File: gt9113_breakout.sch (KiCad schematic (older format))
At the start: 8 parts, among them J1 Conn_01x04_Male, J2 10118194-0001LF, J7 504740-5100, J8 504740-5100, U2 HT7533-1-SOT89

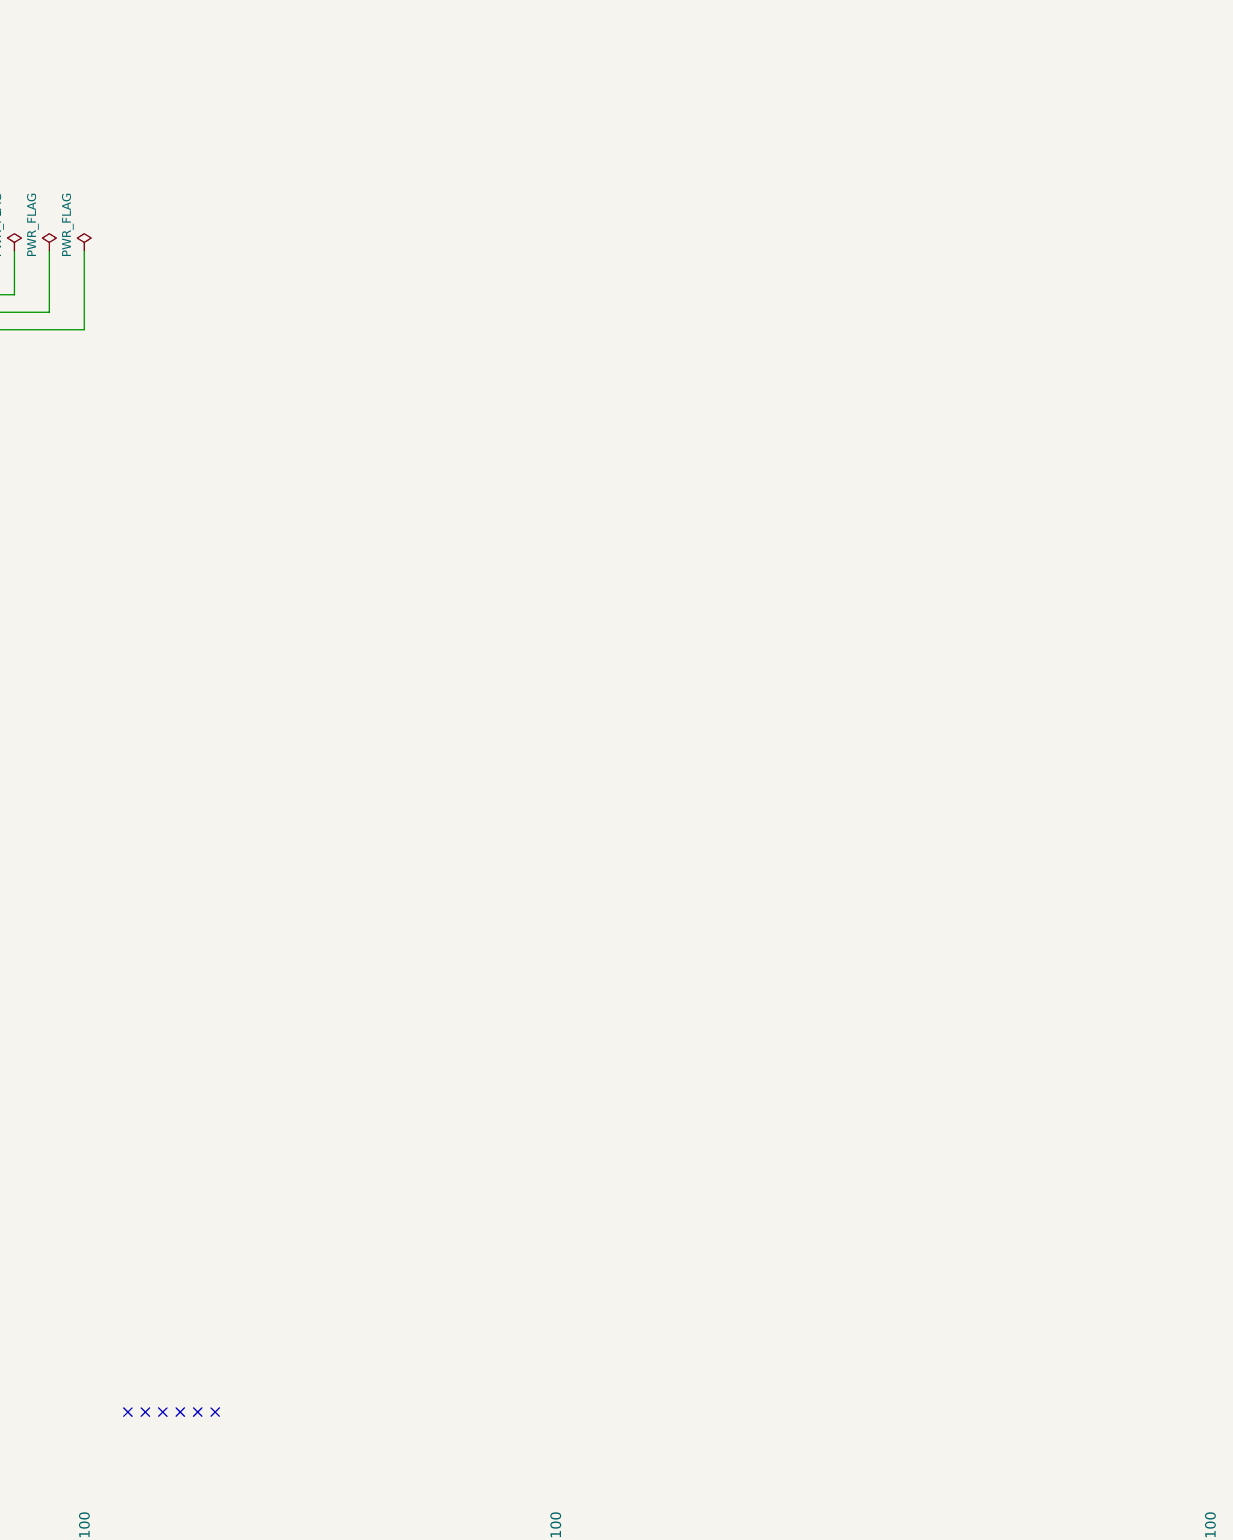
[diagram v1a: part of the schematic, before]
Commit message: Create symbol for GT9113, add it to schematic and attach X0..39 and Y0..29 labels
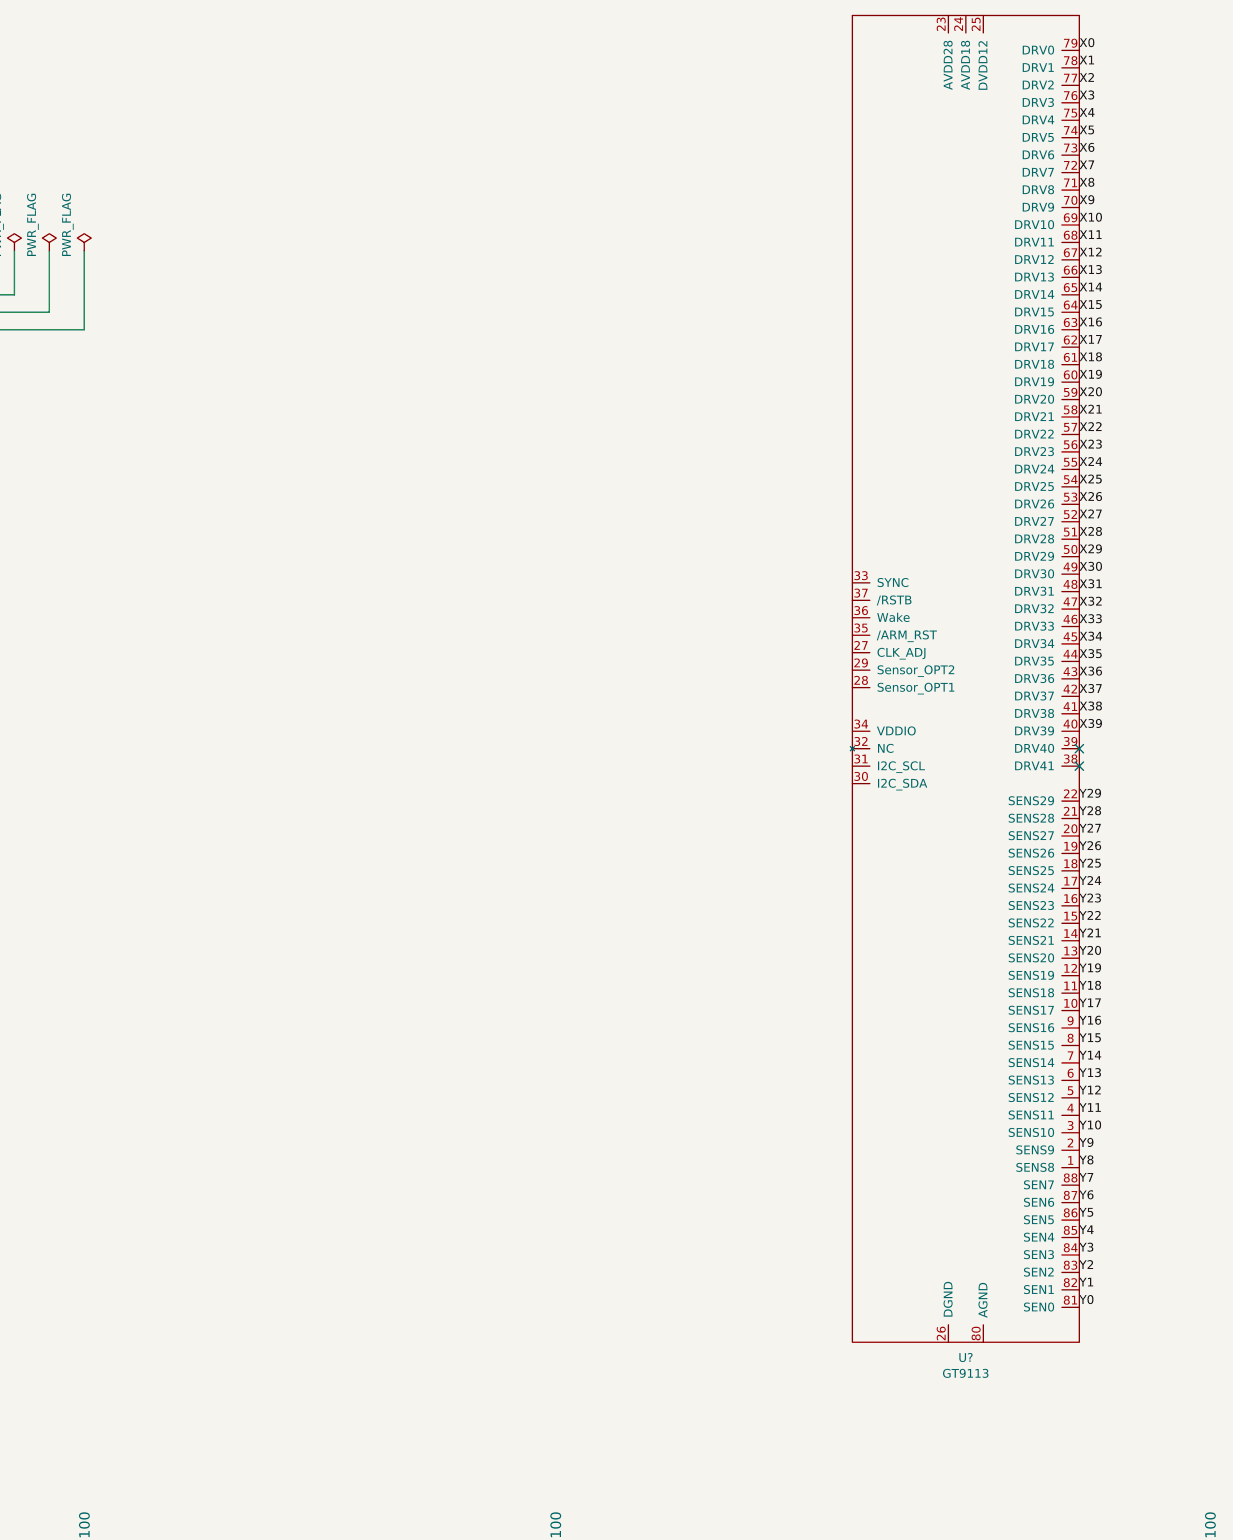
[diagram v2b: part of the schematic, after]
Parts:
- added U?: GT9113, symbol gt9113:GT9113
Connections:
- net X0: now also U?.79 (DRV0)
- net X1: now also U?.78 (DRV1)
- net X10: now also U?.69 (DRV10)
- net X11: now also U?.68 (DRV11)
- net X12: now also U?.67 (DRV12)
- net X13: now also U?.66 (DRV13)
- net X14: now also U?.65 (DRV14)
- net X15: now also U?.64 (DRV15)
- net X16: now also U?.63 (DRV16)
- net X17: now also U?.62 (DRV17)
- net X18: now also U?.61 (DRV18)
- net X19: now also U?.60 (DRV19)
- net X2: now also U?.77 (DRV2)
- net X20: now also U?.59 (DRV20)
- net X21: now also U?.58 (DRV21)
- net X22: now also U?.57 (DRV22)
- net X23: now also U?.56 (DRV23)
- net X24: now also U?.55 (DRV24)
- net X25: now also U?.54 (DRV25)
- net X26: now also U?.53 (DRV26)
- net X27: now also U?.52 (DRV27)
- net X28: now also U?.51 (DRV28)
- net X29: now also U?.50 (DRV29)
- net X3: now also U?.76 (DRV3)
- net X30: now also U?.49 (DRV30)
- net X31: now also U?.48 (DRV31)
- net X32: now also U?.47 (DRV32)
- net X33: now also U?.46 (DRV33)
- net X34: now also U?.45 (DRV34)
- net X35: now also U?.44 (DRV35)
- net X36: now also U?.43 (DRV36)
- net X37: now also U?.42 (DRV37)
- net X38: now also U?.41 (DRV38)
- net X39: now also U?.40 (DRV39)
- net X4: now also U?.75 (DRV4)
- net X5: now also U?.74 (DRV5)
- net X6: now also U?.73 (DRV6)
- net X7: now also U?.72 (DRV7)
- net X8: now also U?.71 (DRV8)
- net X9: now also U?.70 (DRV9)
- net Y0: now also U?.81 (SEN0)
- net Y1: now also U?.82 (SEN1)
- net Y10: now also U?.3 (SENS10)
- net Y11: now also U?.4 (SENS11)
- net Y12: now also U?.5 (SENS12)
- net Y13: now also U?.6 (SENS13)
- net Y14: now also U?.7 (SENS14)
- net Y15: now also U?.8 (SENS15)
- net Y16: now also U?.9 (SENS16)
- net Y17: now also U?.10 (SENS17)
- net Y18: now also U?.11 (SENS18)
- net Y19: now also U?.12 (SENS19)
- net Y2: now also U?.83 (SEN2)
- net Y20: now also U?.13 (SENS20)
- net Y21: now also U?.14 (SENS21)
- net Y22: now also U?.15 (SENS22)
- net Y23: now also U?.16 (SENS23)
- net Y24: now also U?.17 (SENS24)
- net Y25: now also U?.18 (SENS25)
- net Y26: now also U?.19 (SENS26)
- net Y27: now also U?.20 (SENS27)
- net Y28: now also U?.21 (SENS28)
- net Y29: now also U?.22 (SENS29)
- net Y3: now also U?.84 (SEN3)
- net Y4: now also U?.85 (SEN4)
- net Y5: now also U?.86 (SEN5)
- net Y6: now also U?.87 (SEN6)
- net Y7: now also U?.88 (SEN7)
- net Y8: now also U?.1 (SENS8)
- net Y9: now also U?.2 (SENS9)
- no-connect marks 7 -> 3
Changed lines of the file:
@@
 Text Label 12800 11400 3    50   ~ 0
 Y23
-NoConn ~ 5550 9750
-NoConn ~ 5450 9750
-NoConn ~ 5350 9750
-NoConn ~ 5250 9750
-NoConn ~ 5150 9750
-NoConn ~ 5050 9750
 $Comp
 L power:GND #PWR01
@@
 Text Label 950  5550 0    50   ~ 0
 VIN_3.3
+$Comp
+L gt9113:GT9113 U?
+U 1 1 60371774
+P 9850 5550
+F 0 "U?" H 9850 1661 50  0000 C CNN
+F 1 "GT9113" H 9850 1570 50  0000 C CNN
+F 2 "" H 9800 6100 50  0001 C CNN
+F 3 "" H 9800 6100 50  0001 C CNN
+	1    9850 5550
+	1    0    0    -1
+$EndComp
+Text Label 10500 1950 0    50   ~ 0
+X0
+Text Label 10500 2050 0    50   ~ 0
+X1
+Text Label 10500 2150 0    50   ~ 0
+X2
+Text Label 10500 2250 0    50   ~ 0
+X3
+Text Label 10500 2350 0    50   ~ 0
+X4
+Text Label 10500 2450 0    50   ~ 0
+X5
+Text Label 10500 2550 0    50   ~ 0
+X6
+Text Label 10500 2650 0    50   ~ 0
+X7
+Text Label 10500 2750 0    50   ~ 0
+X8
+Text Label 10500 2850 0    50   ~ 0
+X9
+Text Label 10500 2950 0    50   ~ 0
+X10
+Text Label 10500 3050 0    50   ~ 0
+X11
+Text Label 10500 3150 0    50   ~ 0
+X12
+Text Label 10500 3250 0    50   ~ 0
+X13
+Text Label 10500 3350 0    50   ~ 0
+X14
+Text Label 10500 3450 0    50   ~ 0
+X15
+Text Label 10500 3550 0    50   ~ 0
+X16
+Text Label 10500 3650 0    50   ~ 0
+X17
+Text Label 10500 3750 0    50   ~ 0
+X18
+Text Label 10500 3850 0    50   ~ 0
+X19
+Text Label 10500 3950 0    50   ~ 0
+X20
+Text Label 10500 4050 0    50   ~ 0
+X21
+Text Label 10500 4150 0    50   ~ 0
+X22
+Text Label 10500 4250 0    50   ~ 0
+X23
+Text Label 10500 4350 0    50   ~ 0
+X24
+Text Label 10500 4450 0    50   ~ 0
+X25
+Text Label 10500 4550 0    50   ~ 0
+X26
+Text Label 10500 4650 0    50   ~ 0
+X27
+Text Label 10500 4750 0    50   ~ 0
+X28
+Text Label 10500 4850 0    50   ~ 0
+X29
+Text Label 10500 4950 0    50   ~ 0
+X30
+Text Label 10500 5050 0    50   ~ 0
+X31
+Text Label 10500 5150 0    50   ~ 0
+X32
+Text Label 10500 5250 0    50   ~ 0
+X33
+Text Label 10500 5350 0    50   ~ 0
+X34
+Text Label 10500 5450 0    50   ~ 0
+X35
+Text Label 10500 5550 0    50   ~ 0
+X36
+Text Label 10500 5650 0    50   ~ 0
+X37
+Text Label 10500 5750 0    50   ~ 0
+X38
+Text Label 10500 5850 0    50   ~ 0
+X39
+NoConn ~ 10500 5950
+NoConn ~ 10500 6050
+Text Label 10500 9150 0    50   ~ 0
+Y0
+Text Label 10500 9050 0    50   ~ 0
+Y1
+Text Label 10500 8950 0    50   ~ 0
+Y2
+Text Label 10500 8850 0    50   ~ 0
+Y3
+Text Label 10500 8750 0    50   ~ 0
+Y4
+Text Label 10500 8650 0    50   ~ 0
+Y5
+Text Label 10500 8550 0    50   ~ 0
+Y6
+Text Label 10500 8450 0    50   ~ 0
+Y7
+Text Label 10500 8350 0    50   ~ 0
+Y8
+Text Label 10500 8250 0    50   ~ 0
+Y9
+Text Label 10500 8150 0    50   ~ 0
+Y10
+Text Label 10500 8050 0    50   ~ 0
+Y11
+Text Label 10500 7950 0    50   ~ 0
+Y12
+Text Label 10500 7850 0    50   ~ 0
+Y13
+Text Label 10500 7750 0    50   ~ 0
+Y14
+Text Label 10500 7650 0    50   ~ 0
+Y15
+Text Label 10500 7550 0    50   ~ 0
+Y16
+Text Label 10500 7450 0    50   ~ 0
+Y17
+Text Label 10500 7350 0    50   ~ 0
+Y18
+Text Label 10500 7250 0    50   ~ 0
+Y19
+Text Label 10500 7150 0    50   ~ 0
+Y20
+Text Label 10500 7050 0    50   ~ 0
+Y21
+Text Label 10500 6950 0    50   ~ 0
+Y22
+Text Label 10500 6850 0    50   ~ 0
+Y23
+Text Label 10500 6750 0    50   ~ 0
+Y24
+Text Label 10500 6650 0    50   ~ 0
+Y25
+Text Label 10500 6550 0    50   ~ 0
+Y26
+Text Label 10500 6450 0    50   ~ 0
+Y27
+Text Label 10500 6350 0    50   ~ 0
+Y28
+Text Label 10500 6250 0    50   ~ 0
+Y29
 $EndSCHEMATC
